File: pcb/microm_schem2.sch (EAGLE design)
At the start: 77 parts, among them Q1 16 MHz

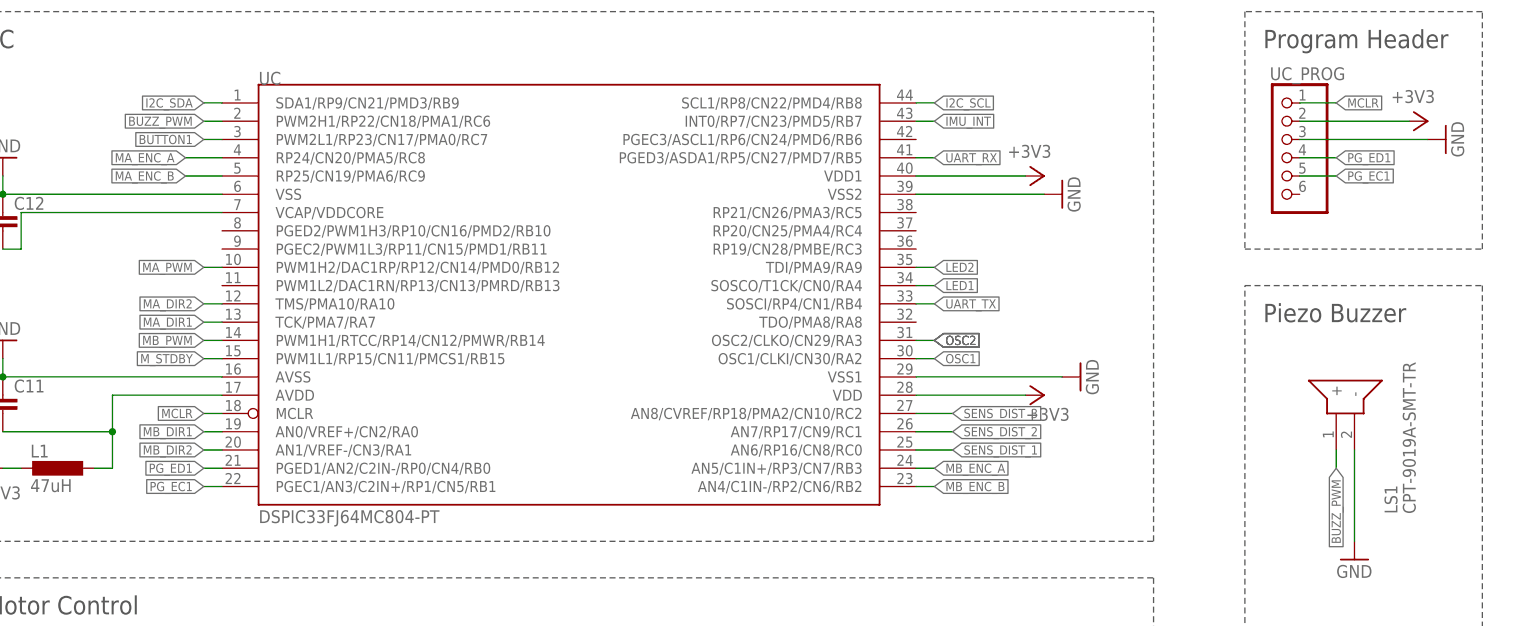
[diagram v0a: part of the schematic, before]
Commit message: Optimizations on pcb, unify via sizes and trace widths.
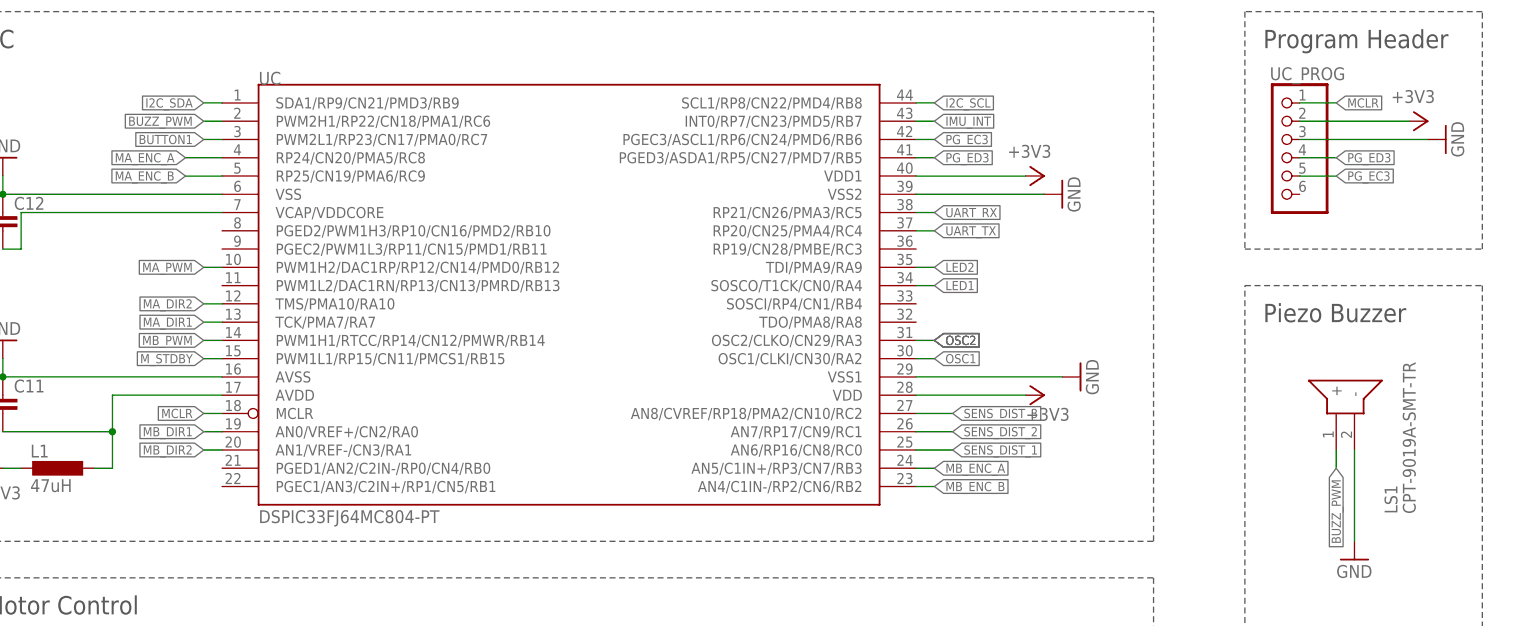
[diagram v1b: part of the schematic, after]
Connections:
- removed net PG_EC1: UC.PGEC1/AN3/C2IN+/RP1/CN5/RB1, UC_PROG.5
- removed net PG_ED1: UC.PGED1/AN2/C2IN-/RP0/CN4/RB0, UC_PROG.4
- new net PG_EC3: UC.PGEC3/ASCL1/RP6/CN24/PMD6/RB6, UC_PROG.5
- new net PG_ED3: UC.PGED3/ASDA1/RP5/CN27/PMD7/RB5, UC_PROG.4
- net UART_RX: now also UC.RP21/CN26/PMA3/RC5; no longer UC.PGED3/ASDA1/RP5/CN27/PMD7/RB5
- net UART_TX: now also UC.RP20/CN25/PMA4/RC4; no longer UC.SOSCI/RP4/CN1/RB4
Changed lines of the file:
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@@
 </segment>
 <segment>
-<pinref part="UC" gate="G$1" pin="SOSCI/RP4/CN1/RB4"/>
-<wire x1="114.3" y1="220.98" x2="116.84" y2="220.98" width="0.1524" layer="91"/>
-<label x="116.84" y="220.98" size="1.27" layer="95" xref="yes"/>
+<pinref part="UC" gate="G$1" pin="RP20/CN25/PMA4/RC4"/>
+<wire x1="114.3" y1="231.14" x2="116.84" y2="231.14" width="0.1524" layer="91"/>
+<label x="116.84" y="231.14" size="1.27" layer="95" xref="yes"/>
 </segment>
 </net>
 <net name="UART_RX" class="0">
-<segment>
-<pinref part="UC" gate="G$1" pin="PGED3/ASDA1/RP5/CN27/PMD7/RB5"/>
-<wire x1="114.3" y1="241.3" x2="116.84" y2="241.3" width="0.1524" layer="91"/>
-<label x="116.84" y="241.3" size="1.27" layer="95" xref="yes"/>
-</segment>
 <segment>
 <pinref part="RX_SEL" gate="A" pin="2"/>
 <wire x1="-116.84" y1="198.12" x2="-109.22" y2="198.12" width="0.1524" layer="91"/>
 <label x="-109.22" y="198.12" size="1.27" layer="95" xref="yes"/>
+</segment>
+<segment>
+<pinref part="UC" gate="G$1" pin="RP21/CN26/PMA3/RC5"/>
+<wire x1="114.3" y1="233.68" x2="116.84" y2="233.68" width="0.1524" layer="91"/>
+<label x="116.84" y="233.68" size="1.27" layer="95" xref="yes"/>
 </segment>
 </net>
@@
 </segment>
 </net>
-<net name="PG_ED1" class="0">
+<net name="PG_ED3" class="0">
 <segment>
 <wire x1="167.64" y1="241.3" x2="172.72" y2="241.3" width="0.1524" layer="91"/>
@@
 </segment>
 <segment>
-<pinref part="UC" gate="G$1" pin="PGED1/AN2/C2IN-/RP0/CN4/RB0"/>
-<wire x1="17.78" y1="198.12" x2="15.24" y2="198.12" width="0.1524" layer="91"/>
-<label x="15.24" y="198.12" size="1.27" layer="95" rot="MR0" xref="yes"/>
-</segment>
-</net>
-<net name="PG_EC1" class="0">
+<pinref part="UC" gate="G$1" pin="PGED3/ASDA1/RP5/CN27/PMD7/RB5"/>
+<wire x1="114.3" y1="241.3" x2="116.84" y2="241.3" width="0.1524" layer="91"/>
+<label x="116.84" y="241.3" size="1.27" layer="95" xref="yes"/>
+</segment>
+</net>
+<net name="PG_EC3" class="0">
 <segment>
 <wire x1="167.64" y1="238.76" x2="172.72" y2="238.76" width="0.1524" layer="91"/>
@@
 </segment>
 <segment>
-<pinref part="UC" gate="G$1" pin="PGEC1/AN3/C2IN+/RP1/CN5/RB1"/>
-<wire x1="17.78" y1="195.58" x2="15.24" y2="195.58" width="0.1524" layer="91"/>
-<label x="15.24" y="195.58" size="1.27" layer="95" rot="MR0" xref="yes"/>
-</segment>
-</net>
+<pinref part="UC" gate="G$1" pin="PGEC3/ASCL1/RP6/CN24/PMD6/RB6"/>
+<wire x1="114.3" y1="243.84" x2="116.84" y2="243.84" width="0.1524" layer="91"/>
+<label x="116.84" y="243.84" size="1.27" layer="95" xref="yes"/>
+</segment>
+</net>

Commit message: More wiring optimizations.
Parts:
- added C23: 100nF, rcl:C-EUC0805
- added LED3, LED4: red, 2mA, 2.1V, led:LEDCHIPLED_0805
- added R14, R15: 680Ω, rcl:R-EU_R0805
- C12: value 10uF, 10-20V, low-esr -> opt
- C13: value 100nF, 10-20V, low-esr -> 10uF, 10-20V, low-esr
- C15: value 20pF, low-esr, ceramic -> 100nF, 10-20V, low-esr
- C17: value 10 uF -> 20pF, low-esr, ceramic
- C20: value 1uF -> 10 uF
- C22: value 100nF -> 1uF
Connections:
- new net LED3: LED3.C, UC.TDI/PMA9/RA9
- new net LED4: LED4.C, UC.RP19/CN28/PMBE/RC3
- new net N$61: LED3.A, R14.2
- new net N$62: LED4.A, R15.2
- net +3V3: now also C15.1, R14.1, R15.1; no longer C13.1
- net +5V: now also C20.1; no longer C17.1
- net BT_PROG: now also C22.1; no longer C21.1
- net BT_RESET: now also C21.1; no longer C20.1
- net GND: now also C13.1, C23.2; no longer C13.2
- net LED1: now also UC.SOSCI/RP4/CN1/RB4; no longer UC.SOSCO/T1CK/CN0/RA4
- net LED2: now also UC.SOSCO/T1CK/CN0/RA4; no longer UC.TDI/PMA9/RA9
- net MB_ENC_A: now also UC.PGEC1/AN3/C2IN+/RP1/CN5/RB1; no longer UC.AN5/C1IN+/RP3/CN7/RB3
- net MB_ENC_B: now also UC.PGED1/AN2/C2IN-/RP0/CN4/RB0; no longer UC.AN4/C1IN-/RP2/CN6/RB2
- net N$5: now also C12.2
- net N$6: now also C23.1; no longer C22.1
- net OSC1: now also C16.1; no longer C15.1
- net OSC2: now also C17.1; no longer C16.1
- net SENS_DIST_1: now also UC.AN5/C1IN+/RP3/CN7/RB3; no longer UC.AN6/RP16/CN8/RC0
- net SENS_DIST_2: now also UC.AN6/RP16/CN8/RC0; no longer UC.AN7/RP17/CN9/RC1
- net SENS_DIST_3: now also UC.AN4/C1IN-/RP2/CN6/RB2; no longer UC.AN8/CVREF/RP18/PMA2/CN10/RC2
- net UART_RX: now also UC.RP20/CN25/PMA4/RC4; no longer UC.RP21/CN26/PMA3/RC5
- net UART_TX: now also UC.RP21/CN26/PMA3/RC5; no longer UC.RP20/CN25/PMA4/RC4
- net VCAP/VDDCORE: now also C13.2; no longer C12.2
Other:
- moved on the sheet: C12, C13, C14, C15, C16, C17, C18, C19, C20, C21, C22

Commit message: Few more optimizations.
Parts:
- R10, R9: value 10kΩ -> 2.2kΩ
- R11: value 1kΩ -> 10kΩ
- R13: value 10kΩ -> 1kΩ
- R14, R15: value 680Ω -> 10kΩ
- R6: value 180Ω -> 680Ω
- R7: value 2.2kΩ -> 680Ω
- R8: value 2.2kΩ -> 180Ω
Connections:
- removed net UART_BT_RX_IND: UART_BT.P1_6
- net +3V3: now also R10.1, R14.2, R15.2, R6.1, R9.1; no longer R10.2, R13.2, R14.1, R15.1, R8.1
- net BT_PROG: now also R14.1; no longer R12.1
- net BT_RESET: now also R15.1; no longer R13.1
- net BT_STATUS: now also R8.1; no longer R6.1
- net BUTTON1: now also R13.2; no longer R11.2
- net I2C_SCL: now also R9.2; no longer R7.2
- net I2C_SDA: now also R10.2; no longer R8.2
- net MCLR: now also R11.1; no longer R9.1
- net N$1: now also R8.2; no longer R6.2
- net N$6: now also R12.1, R13.1; no longer R10.1, R11.1
- net N$61: now also R6.2; no longer R14.2
- net N$62: now also R7.2; no longer R15.2
- net N$7: now also R11.2; no longer R9.2
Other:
- moved on the sheet: R10, R11, R12, R13, R14, R15, R6, R7, R8, R9

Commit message: Further refinements.
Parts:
- removed I2C: (no value), pinhead:PINHD-1X4
- added C24: 1uF, rcl:C-EUC0805
- added OLED: (no value), pinhead:PINHD-1X4
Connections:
- net +3V3: now also C24.1, OLED.2; no longer I2C.4
- net GND: now also C24.2, OLED.1; no longer I2C.3
- net I2C_SCL: now also OLED.3; no longer I2C.1
- net I2C_SDA: now also OLED.4; no longer I2C.2
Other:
- note added: "I2C Pull-Up Resistors Only if lower resistance is needed"
- note added: "OLED Display"
- note removed: "Debug Interfaces"
- note removed: "I2C Pull-Up Resistors Only in case lower resistance is needed"
- note removed: "TODO:"
- moved on the sheet: R10, R9, RX_SEL, UART

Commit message: Add GPIO header for remaining pins.
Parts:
- added GPIO1: (no value), pinhead:PINHD-1X3
- added GPIO2: (no value), pinhead:PINHD-1X2
- added LED5: red, 2mA, 2.1V, led:LEDCHIPLED_0805
- added R16: 10kΩ, rcl:R-EU_R0805
- R11: value 10kΩ -> 2.2kΩ
- R13: value 1kΩ -> 10kΩ
- R14: value 10kΩ -> 1kΩ
- R8: value 180Ω -> 680Ω
- R9: value 2.2kΩ -> 180Ω
- renumbered UC to μC
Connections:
- new net GPIO_11: GPIO2.2, μC.PWM1L2/DAC1RN/RP13/CN13/PMRD/RB13
- new net GPIO_26: GPIO1.1, μC.AN7/RP17/CN9/RC1
- new net GPIO_27: GPIO1.2, μC.AN8/CVREF/RP18/PMA2/CN10/RC2
- new net GPIO_32: GPIO1.3, μC.TDO/PMA8/RA8
- new net GPIO_9: GPIO2.1, μC.PGEC2/PWM1L3/RP11/CN15/PMD1/RB11
- new net LED5: LED5.C, μC.PGED2/PWM1H3/RP10/CN16/PMD2/RB10
- new net N$63: LED5.A, R8.2
- net +3V3: now also R11.1, R13.2, R16.2, R8.1; no longer R12.2, R14.2, R9.1
- net BT_PROG: now also R15.1; no longer R14.1
- net BT_RESET: now also R16.1; no longer R15.1
- net BT_STATUS: now also R9.1; no longer R8.1
- net BUTTON1: now also R14.2; no longer R13.2
- net I2C_SCL: now also R10.2; no longer R9.2
- net I2C_SDA: now also R11.2; no longer R10.2
- net MCLR: now also R12.1; no longer R11.1
- net N$1: now also R9.2; no longer R8.2
- net N$6: now also R14.1; no longer R12.1
- net N$7: now also R12.2; no longer R11.2
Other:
- note added: "GPIO"
- moved on the sheet: R10, R11, R12, R13, R14, R15, R8, R9

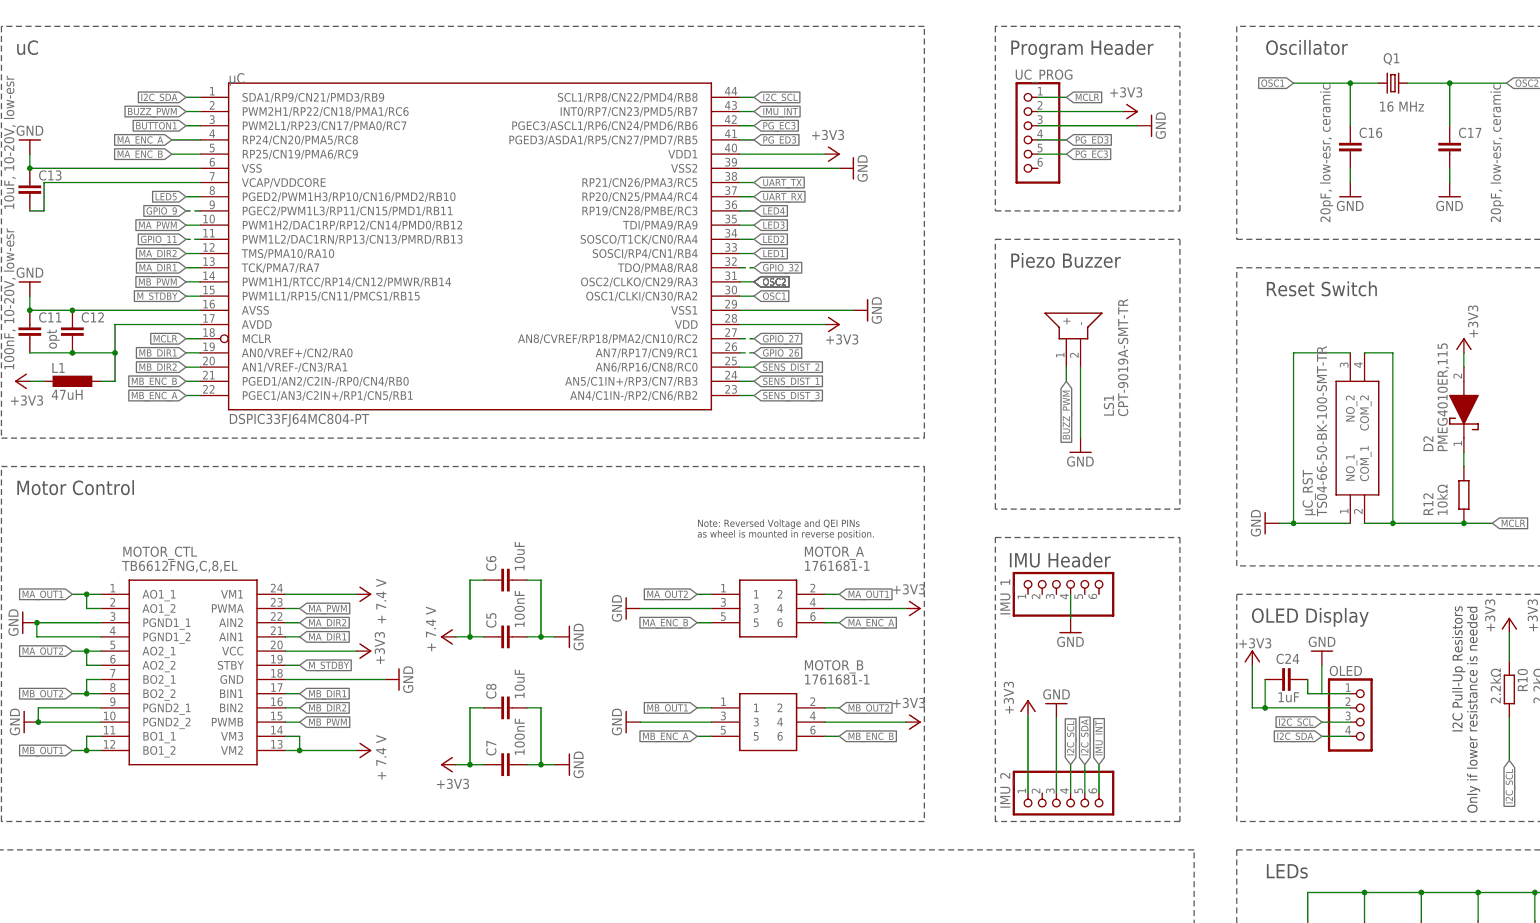
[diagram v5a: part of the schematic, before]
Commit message: Finalize traces.
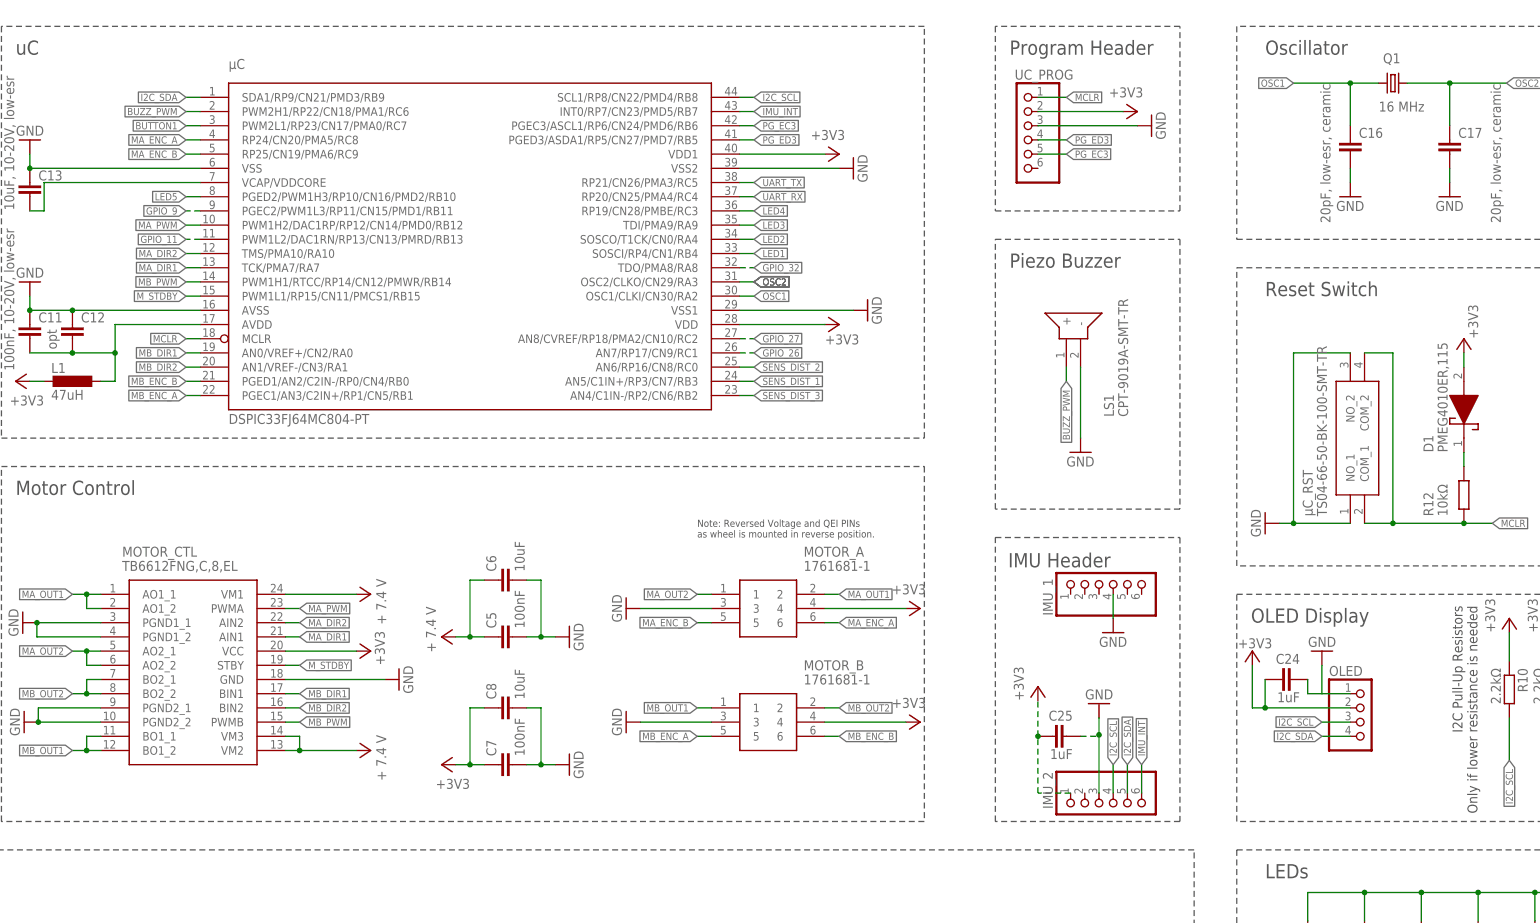
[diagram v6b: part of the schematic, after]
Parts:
- added C25: 1uF, rcl:C-EUC0805
- renumbered D2 to D1
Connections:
- net +3V3: now also C25.1
- net GND: now also C25.2
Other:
- moved on the sheet: IMU_1, IMU_2

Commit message: Add TUM logo and update values.
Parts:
- C13: value 10uF, 10-20V, low-esr -> 10uF, 10-20V, low-esr, tantalum
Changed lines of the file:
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@@
 <part name="C3" library="rcl" library_urn="urn:adsk.eagle:library:334" deviceset="C-EU" device="C0805" package3d_urn="urn:adsk.eagle:package:23617/2" value="10uF, tantalum"/>
 <part name="C4" library="rcl" library_urn="urn:adsk.eagle:library:334" deviceset="C-EU" device="C0805" package3d_urn="urn:adsk.eagle:package:23617/2" value="22uF, tantalum, esr 0.3-22Ω"/>
-<part name="C13" library="rcl" library_urn="urn:adsk.eagle:library:334" deviceset="C-EU" device="C0805" package3d_urn="urn:adsk.eagle:package:23617/2" value="10uF, 10-20V, low-esr"/>
+<part name="C13" library="rcl" library_urn="urn:adsk.eagle:library:334" deviceset="C-EU" device="C0805" package3d_urn="urn:adsk.eagle:package:23617/2" value="10uF, 10-20V, low-esr, tantalum"/>
 <part name="C10" library="rcl" library_urn="urn:adsk.eagle:library:334" deviceset="C-EU" device="C0805" package3d_urn="urn:adsk.eagle:package:23617/2" value="100nF, 10-20V, low-esr"/>
 <part name="C14" library="rcl" library_urn="urn:adsk.eagle:library:334" deviceset="C-EU" device="C0805" package3d_urn="urn:adsk.eagle:package:23617/2" value="100nF, 10-20V, low-esr"/>
@@
 <instance part="C13" gate="G$1" x="-12.7" y="233.68" smashed="yes">
 <attribute name="NAME" x="-11.176" y="234.061" size="1.778" layer="95"/>
-<attribute name="VALUE" x="-15.494" y="228.727" size="1.778" layer="96" rot="R90"/>
+<attribute name="VALUE" x="-15.748" y="225.679" size="1.778" layer="96" rot="R90"/>
 </instance>
 <instance part="C10" gate="G$1" x="127" y="60.96" smashed="yes">

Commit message: Fix LED resistors.
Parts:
- 3.3V, 5V, 7.4V: value green, 2mA, 3V -> green, 2mA, 2.2V
- BT_CON: value blue, 2mA, 3V -> blue, 2mA, 2.2V
- C18, C19, C20: value 10 uF -> 10uF
- LED1, LED2, LED3, LED4, LED5: value red, 2mA, 2.1V -> red, 2mA, 1.5V
- R2: value 1.2kΩ -> 1.5kΩ
- R3, R9: value 180Ω -> 560Ω
- R4, R5, R6, R7, R8: value 680Ω -> 1kΩ
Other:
- moved on the sheet: C18, C19, C20, SENS_DIST_1, SENS_DIST_2, SENS_DIST_3
